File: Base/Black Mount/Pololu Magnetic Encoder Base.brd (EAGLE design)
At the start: 26.7 x 33.7 mm, 0 parts

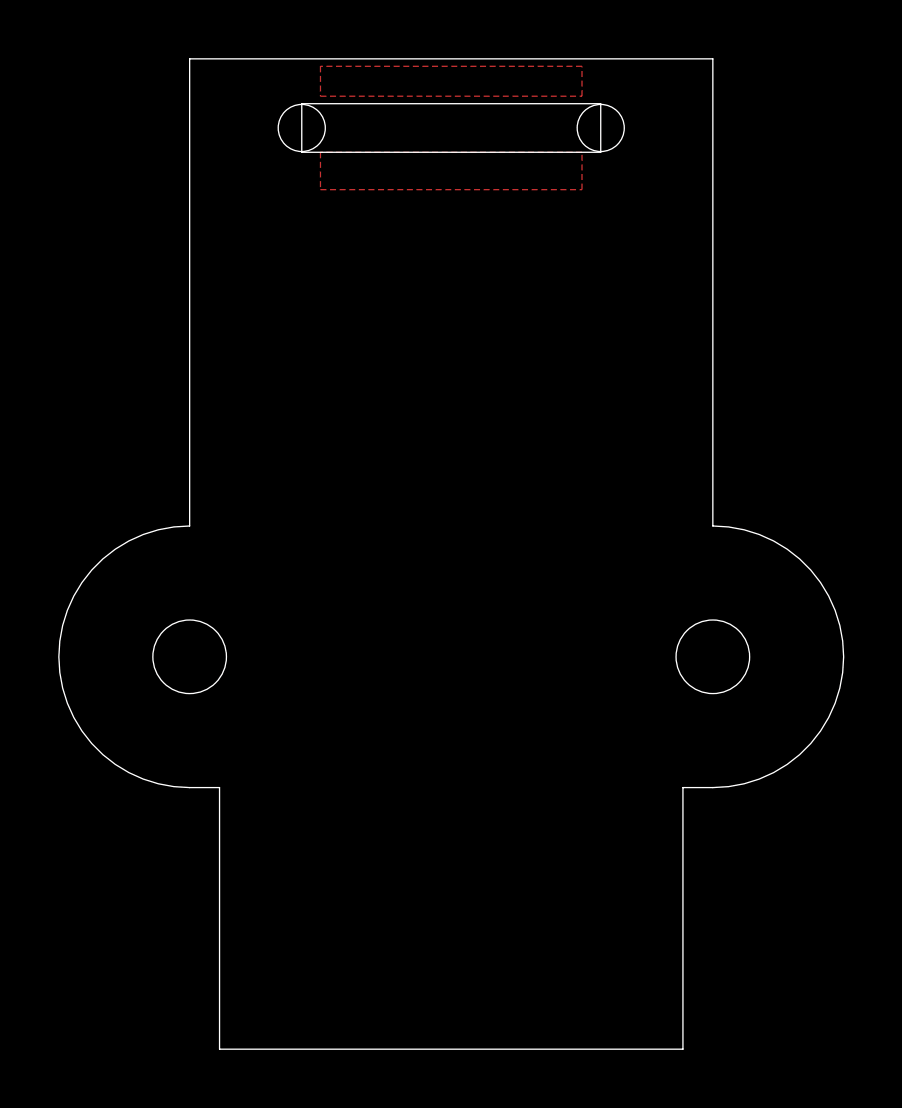
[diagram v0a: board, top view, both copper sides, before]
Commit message: Messing with encoders. Created base plate for Black Mount Created two PCBs for base-less/floating encoder
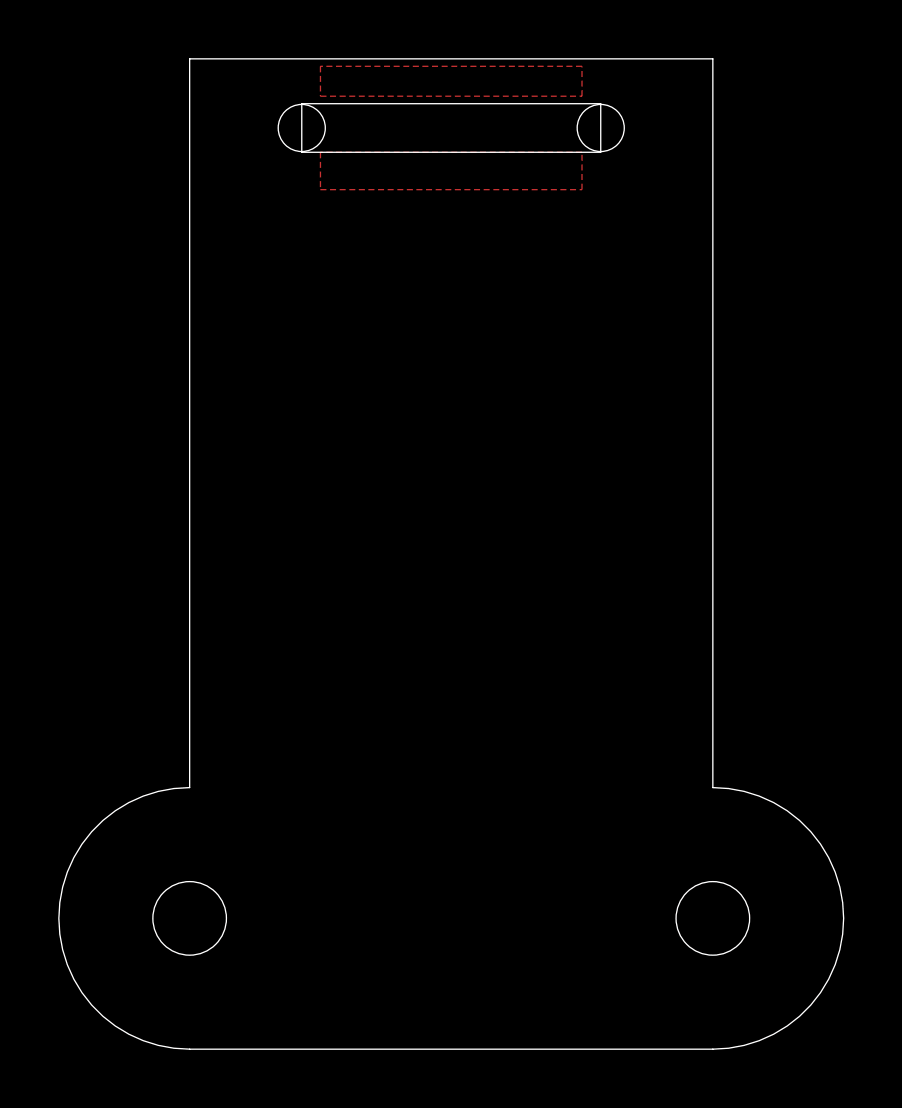
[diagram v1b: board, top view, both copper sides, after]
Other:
- outline, holes or cut-outs redrawn
- board text added: "AnomalousMaker.com"
- board text removed: "innovativemaker.com"
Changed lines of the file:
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@@
 <?xml version="1.0" encoding="utf-8"?>
 <!DOCTYPE eagle SYSTEM "eagle.dtd">
-<eagle version="6.3">
+<eagle version="6.4">
 <drawing>
 <settings>
@@
 <board>
 <plain>
-<wire x1="6.096" y1="0" x2="21.844" y2="0" width="0" layer="20"/>
-<wire x1="21.844" y1="0" x2="21.844" y2="8.89" width="0" layer="20"/>
-<wire x1="22.86" y1="17.78" x2="22.86" y2="33.655" width="0" layer="20"/>
+<wire x1="5.08" y1="0" x2="22.86" y2="0" width="0" layer="20"/>
+<wire x1="22.86" y1="8.89" x2="22.86" y2="33.655" width="0" layer="20"/>
 <wire x1="22.86" y1="33.655" x2="5.08" y2="33.655" width="0" layer="20"/>
-<wire x1="5.08" y1="33.655" x2="5.08" y2="17.78" width="0" layer="20"/>
-<wire x1="6.096" y1="8.89" x2="6.096" y2="0" width="0" layer="20"/>
-<hole x="5.08" y="13.335" drill="2.5"/>
-<hole x="22.86" y="13.335" drill="2.5"/>
+<wire x1="5.08" y1="33.655" x2="5.08" y2="8.89" width="0" layer="20"/>
+<hole x="5.08" y="4.445" drill="2.5"/>
+<hole x="22.86" y="4.445" drill="2.5"/>
 <wire x1="8.89" y1="30.48" x2="19.05" y2="30.48" width="0" layer="20"/>
 <wire x1="19.05" y1="30.48" x2="19.05" y2="32.131" width="0" layer="20"/>
@@
 <hole x="8.89" y="31.3055" drill="1.6"/>
 <hole x="19.05" y="31.3055" drill="1.6"/>
-<text x="8.255" y="22.86" size="1.778" layer="51" font="vector" ratio="12">3.3v</text>
-<text x="8.255" y="20.32" size="1.778" layer="51" font="vector" ratio="12">GND</text>
-<text x="18.415" y="22.86" size="1.778" layer="51" font="vector" ratio="12">A</text>
-<text x="18.415" y="20.32" size="1.778" layer="51" font="vector" ratio="12">B</text>
-<text x="13.335" y="22.86" size="1.778" layer="52" font="vector" ratio="12" rot="MR0">3.3v</text>
-<text x="13.335" y="20.32" size="1.778" layer="52" font="vector" ratio="12" rot="MR0">GND</text>
-<text x="19.685" y="20.32" size="1.778" layer="52" font="vector" ratio="12" rot="MR0">B</text>
-<text x="19.685" y="22.86" size="1.778" layer="52" font="vector" ratio="12" rot="MR0">A</text>
-<wire x1="5.08" y1="17.78" x2="5.08" y2="8.89" width="0" layer="20" curve="180"/>
-<wire x1="22.86" y1="17.78" x2="22.86" y2="8.89" width="0" layer="20" curve="-180"/>
-<wire x1="6.096" y1="8.89" x2="5.08" y2="8.89" width="0" layer="20"/>
-<wire x1="21.844" y1="8.89" x2="22.86" y2="8.89" width="0" layer="20"/>
+<text x="8.255" y="26.67" size="1.778" layer="51" font="vector" ratio="12">3.3v</text>
+<text x="8.255" y="24.13" size="1.778" layer="51" font="vector" ratio="12">GND</text>
+<text x="18.415" y="26.67" size="1.778" layer="51" font="vector" ratio="12">A</text>
+<text x="18.415" y="24.13" size="1.778" layer="51" font="vector" ratio="12">B</text>
+<text x="13.335" y="26.67" size="1.778" layer="52" font="vector" ratio="12" rot="MR0">3.3v</text>
+<text x="13.335" y="24.13" size="1.778" layer="52" font="vector" ratio="12" rot="MR0">GND</text>
+<text x="19.685" y="24.13" size="1.778" layer="52" font="vector" ratio="12" rot="MR0">B</text>
+<text x="19.685" y="26.67" size="1.778" layer="52" font="vector" ratio="12" rot="MR0">A</text>
+<wire x1="5.08" y1="8.89" x2="5.08" y2="0" width="0" layer="20" curve="180"/>
+<wire x1="22.86" y1="8.89" x2="22.86" y2="0" width="0" layer="20" curve="-180"/>
 <rectangle x1="9.525" y1="32.131" x2="18.415" y2="33.401" layer="29"/>
 <rectangle x1="9.525" y1="29.21" x2="18.415" y2="30.48" layer="29" rot="R180"/>
 <text x="13.97" y="1.905" size="0.8128" layer="52" font="vector" ratio="12" rot="MR0" align="bottom-center">Cruz Monrreal II</text>
-<text x="13.97" y="0.635" size="0.8128" layer="52" font="vector" ratio="12" rot="MR0" align="bottom-center">innovativemaker.com</text>
+<text x="13.97" y="0.635" size="0.8128" layer="52" font="vector" ratio="12" rot="MR0" align="bottom-center">AnomalousMaker.com</text>
 </plain>
 <attributes>
